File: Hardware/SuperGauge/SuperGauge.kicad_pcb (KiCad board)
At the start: 2 copper layers, 51 x 51 mm, 1 part

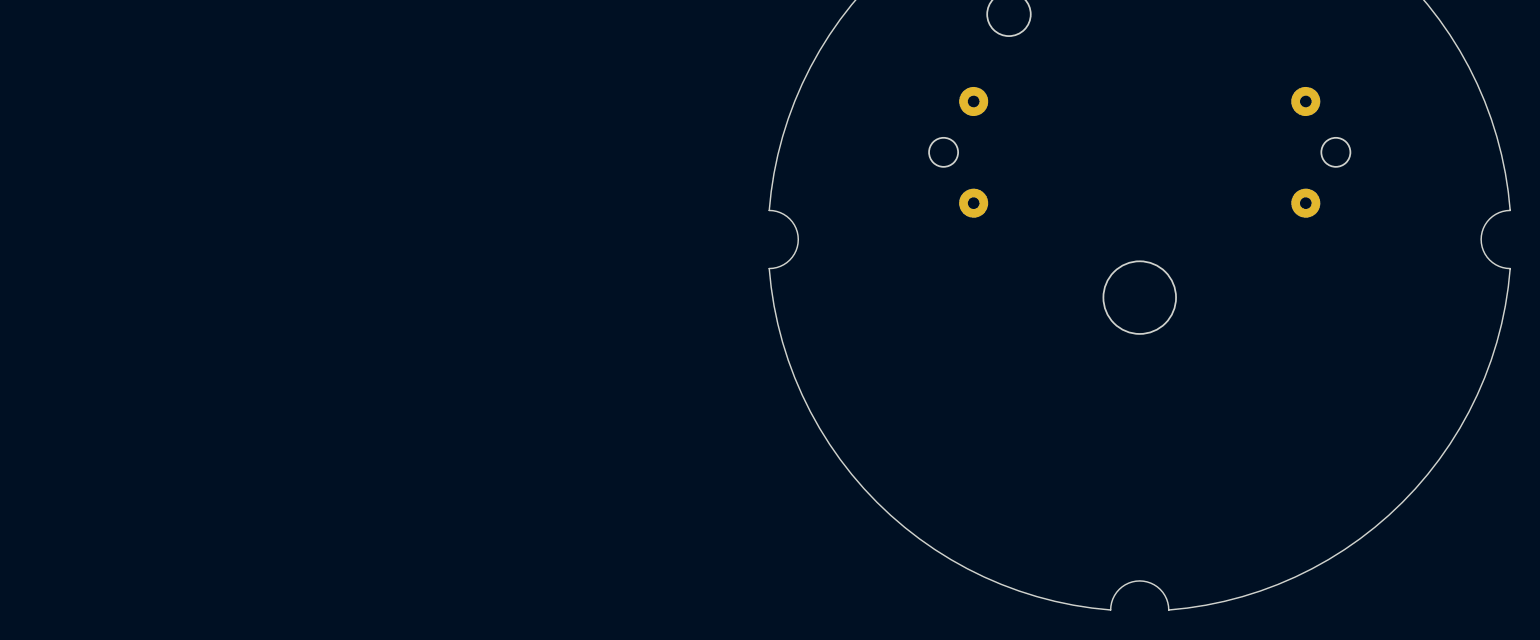
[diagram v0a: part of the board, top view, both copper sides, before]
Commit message: Added in MCU
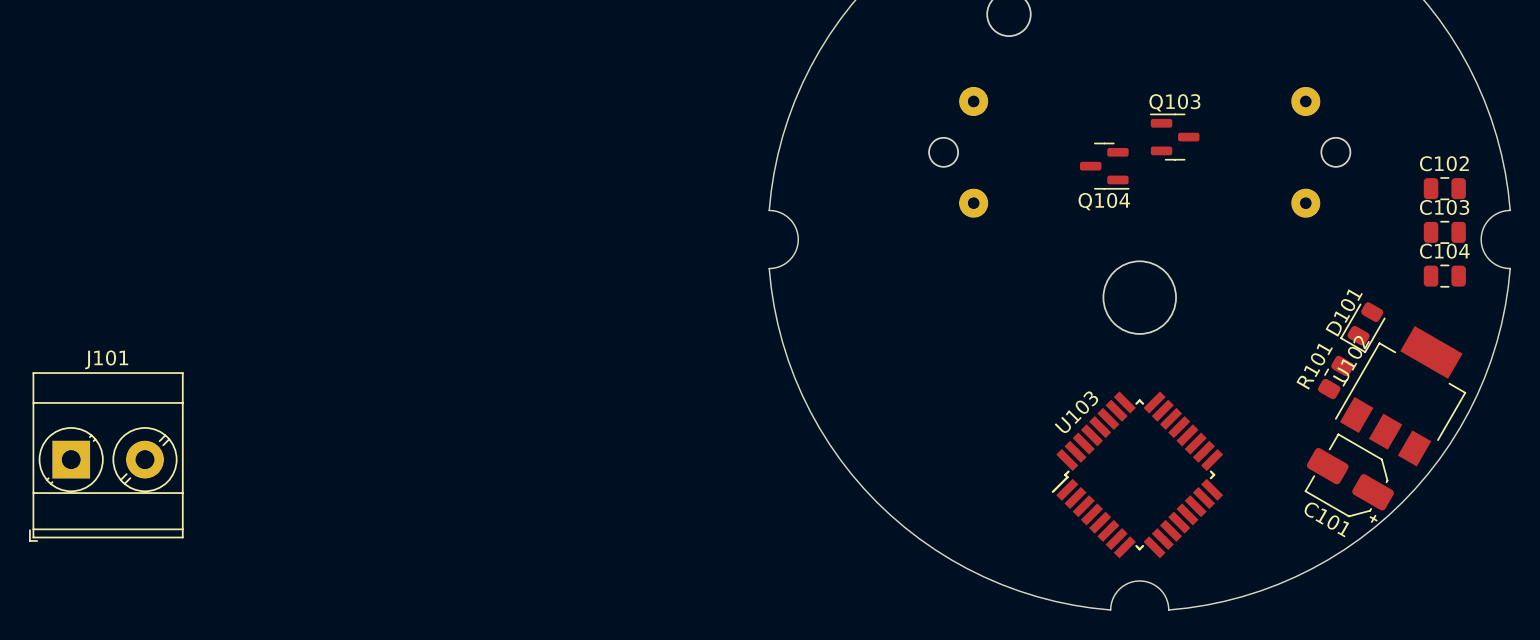
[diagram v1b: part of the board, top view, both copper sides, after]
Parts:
- added C101: 10uf, Capacitor_SMD:CP_Elec_4x3, F.Cu at (164.5, 116.5)
- added C102: 100nF, Capacitor_SMD:C_0805_2012Metric, F.Cu at (171.0, 96.5)
- added C103: 100nF, Capacitor_SMD:C_0805_2012Metric, F.Cu at (171.0, 99.5)
- added C104: 1uF, Capacitor_SMD:C_0805_2012Metric, F.Cu at (171.0, 102.5)
- added D101: PWR, LED_SMD:LED_0805_2012Metric, F.Cu at (165.5, 105.8)
- added J101: 19V Input, TerminalBlock_Phoenix:TerminalBlock_Phoenix_MKDS-3-2-5.08_1x02_P5.08mm_Horizontal, F.Cu at (76.5, 115.2)
- added Q103: MMBT3906, Package_TO_SOT_SMD:SOT-23, F.Cu at (152.4, 93.0)
- added Q104: MMBT3906, Package_TO_SOT_SMD:SOT-23, F.Cu at (147.6, 95.0)
- added R101: 1K, Resistor_SMD:R_0805_2012Metric, F.Cu at (163.5, 109.5)
- added U102: NCV1117ST50T3G, Package_TO_SOT_SMD:SOT-223, F.Cu at (168.5, 110.5)
- added U103: ATmega16U2-A, Package_QFP:TQFP-32_7x7mm_P0.8mm, F.Cu at (150.0, 116.2)
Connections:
- U101 pad 1: unconnected-(U101-Pad1) -> Net-(Q103-C)
- U101 pad 2: unconnected-(U101-Pad2) -> GND
- U101 pad 3: unconnected-(U101-Pad3) -> Net-(Q104-C)
- U101 pad 4: unconnected-(U101-Pad4) -> GND

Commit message: More stuff
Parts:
- removed J101: 19V Input, TerminalBlock_Phoenix:TerminalBlock_Phoenix_MKDS-3-2-5.08_1x02_P5.08mm_Horizontal
- added D102: BACKLIGHTING, LED_THT:LED_D5.0mm_Clear, B.Cu at (129.0, 95.0)
- added D103: BACKLIGHTING, LED_THT:LED_D5.0mm_Clear, B.Cu at (171.0, 95.0)
- added H101: MountingHole, MountingHole:MountingHole_2.5mm, F.Cu at (130.0, 105.0)
- added H102: MountingHole, MountingHole:MountingHole_2.5mm, F.Cu at (170.0, 105.0)
- added J102: MainConn, Connector_JST:JST_EH_B5B-EH-A_1x05_P2.50mm_Vertical, F.Cu at (138.5, 118.5)
- added R102: 1K, Resistor_SMD:R_0805_2012Metric, F.Cu at (132.5, 92.5)
- added R103: 1K, Resistor_SMD:R_0805_2012Metric, F.Cu at (167.5, 92.0)
- U103: value ATmega16U2-A -> ATmega16U2
- moved C101 36.7 mm to (146.5, 84.5), turned to 180 degrees
- moved U102 31.6 mm to (154.8, 82.0), turned to 0 degrees
- moved C104 31.1 mm to (149.0, 80.5), turned to 90 degrees
- moved C102 20.8 mm to (152.5, 87.0)
- moved C103 20.3 mm to (155.0, 112.0), turned to -45 degrees
- moved D101 3.69 mm to (168.5, 108.0), turned to 180 degrees
- moved R101 2.12 mm to (165.0, 108.0), turned to 0 degrees
- turned U103 to -135 degrees
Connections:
- net Net-(J101-Pin_2) renamed +12V
- U103 pad 4: unconnected-(U103-VCC-Pad4) -> +5V
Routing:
- added copper zone on B.Cu, net GND
- added copper zone on F.Cu, net GND
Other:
- board text added: "12V 5V SDA SCL GND"

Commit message: More PCB stuff
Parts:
- added C105: 22pf, Capacitor_SMD:C_0603_1608Metric, F.Cu at (145.2, 109.5)
- added C106: 22pf, Capacitor_SMD:C_0603_1608Metric, F.Cu at (147.5, 107.3)
- added C107: 1u, Capacitor_SMD:C_0805_2012Metric, F.Cu at (191.0, 116.9)
- added D104: STAT, LED_SMD:LED_0805_2012Metric, F.Cu at (195.5, 110.9)
- added J101: USBC, Connector_USB:USB_C_Receptacle_XKB_U262-16XN-4BVC11, F.Cu at (164.5, 115.0)
- added R104: 1K, Resistor_SMD:R_0805_2012Metric, F.Cu at (186.6, 110.9)
- added R106: 5K1, Resistor_SMD:R_0805_2012Metric, F.Cu at (186.6, 116.8)
- added R107: 5K1, Resistor_SMD:R_0805_2012Metric, F.Cu at (186.6, 119.7)
- added Y101: Crystal_GND24, Crystal:Crystal_SMD_3225-4Pin_3.2x2.5mm, F.Cu at (144.4, 106.1)
- moved C103 11.3 mm to (143.8, 111.8), turned to 135 degrees
- moved D101 8.01 mm to (168.1, 100.0)
- moved R101 8.01 mm to (164.6, 100.0)
- moved J102 0.86 mm to (138.1, 119.2)
- moved U103 0.20 mm to (150.0, 116.0), turned to -45 degrees
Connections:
- U103 pad 1: unconnected-(U103-XTAL1-Pad1) -> /XTAL1
- U103 pad 2: unconnected-(U103-PC0/XTAL2-Pad2) -> /XTAL2
- U103 pad 27: unconnected-(U103-UCAP-Pad27) -> Net-(U103-UCAP)
- U103 pad 29: unconnected-(U103-D+-Pad29) -> /USB+
- U103 pad 30: unconnected-(U103-D--Pad30) -> /USB-
- U103 pad 32: unconnected-(U103-AVCC-Pad32) -> +5V
- U103 pad 6: unconnected-(U103-PD0-Pad6) -> Net-(U103-PD0)
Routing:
- net /XTAL1: track 0.00 -> 8.82 mm
- net /XTAL2: track 0.00 -> 5.85 mm
- net GND: track 0.00 -> 3.67 mm, vias 0 -> 5

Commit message: Stuff
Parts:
- removed H101, H102: MountingHole, MountingHole:MountingHole_2.5mm
- added G***: LOGO, KenwoodFox:KITSUNE_LOGO, B.Cu at (146.0, 118.0)
- added J103: Tag Connect, Connector:Tag-Connect_TC2050-IDC-FP_2x05_P1.27mm_Vertical, B.Cu at (130.9, 102.0)
- added R105: 22R, Resistor_SMD:R_0805_2012Metric, F.Cu at (160.6, 109.6)
- added R108: 22R, Resistor_SMD:R_0805_2012Metric, F.Cu at (159.2, 111.0)
- added R109: 10k, Resistor_SMD:R_0805_2012Metric, F.Cu at (156.0, 119.5)
- moved C107 35.0 mm to (156.2, 112.8), turned to -45 degrees
- moved D104 29.0 mm to (168.2, 101.0), turned to 180 degrees
- moved R107 26.6 mm to (160.0, 119.8), turned to 135 degrees
- moved R104 24.0 mm to (164.7, 101.0)
- moved R106 18.4 mm to (169.2, 110.5), turned to 135 degrees
- moved D101 1.26 mm to (168.2, 98.8)
- moved R101 1.26 mm to (164.7, 98.8)
- moved Q104 0.14 mm to (147.7, 94.8)
- moved J102 0.07 mm to (138.1, 119.3)
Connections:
- U103 pad 15: unconnected-(U103-PB1-Pad15) -> /ICSP_SCK
- U103 pad 16: unconnected-(U103-PB2-Pad16) -> /ICSP_MOSI
- U103 pad 17: unconnected-(U103-PB3-Pad17) -> /ICSP_MISO
- U103 pad 24: unconnected-(U103-PC1/~{RESET}-Pad24) -> /ICSP_RST
- U103 pad 29: /USB+ -> Net-(U103-D+)
- U103 pad 30: /USB- -> Net-(U103-D-)
- U103 pad 31: unconnected-(U103-UVCC-Pad31) -> +5V
- U103 pad 7: unconnected-(U103-PD1-Pad7) -> /L1
- U103 pad 8: unconnected-(U103-PD2-Pad8) -> /L2
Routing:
- net +5V: track 0.00 -> 109.5 mm, vias 0 -> 5
- net /ICSP_RST: track 0.00 -> 49.9 mm, vias 0 -> 1
- net /ICSP_MISO: track 0.00 -> 33.8 mm, vias 0 -> 3
- net /ICSP_SCK: track 0.00 -> 32.4 mm, vias 0 -> 1
- net /ICSP_MOSI: track 0.00 -> 29.2 mm, vias 0 -> 3
- net Net-(U103-D+): track 0.00 -> 12.5 mm, vias 0 -> 2
- net Net-(U103-D-): track 0.00 -> 12.1 mm, vias 0 -> 2
- net Net-(J101-CC1): track 0.00 -> 7.86 mm
- net Net-(J101-CC2): track 0.00 -> 7.36 mm
- net /USB+: track 0.00 -> 4.81 mm
- net /USB-: track 0.00 -> 3.95 mm
- net GND: track 3.67 -> 3.02 mm, vias 5 -> 17
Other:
- outline, holes or cut-outs redrawn
- board text added: "Super Gauge ${FULL_REVISION}"
- board text added: "←"

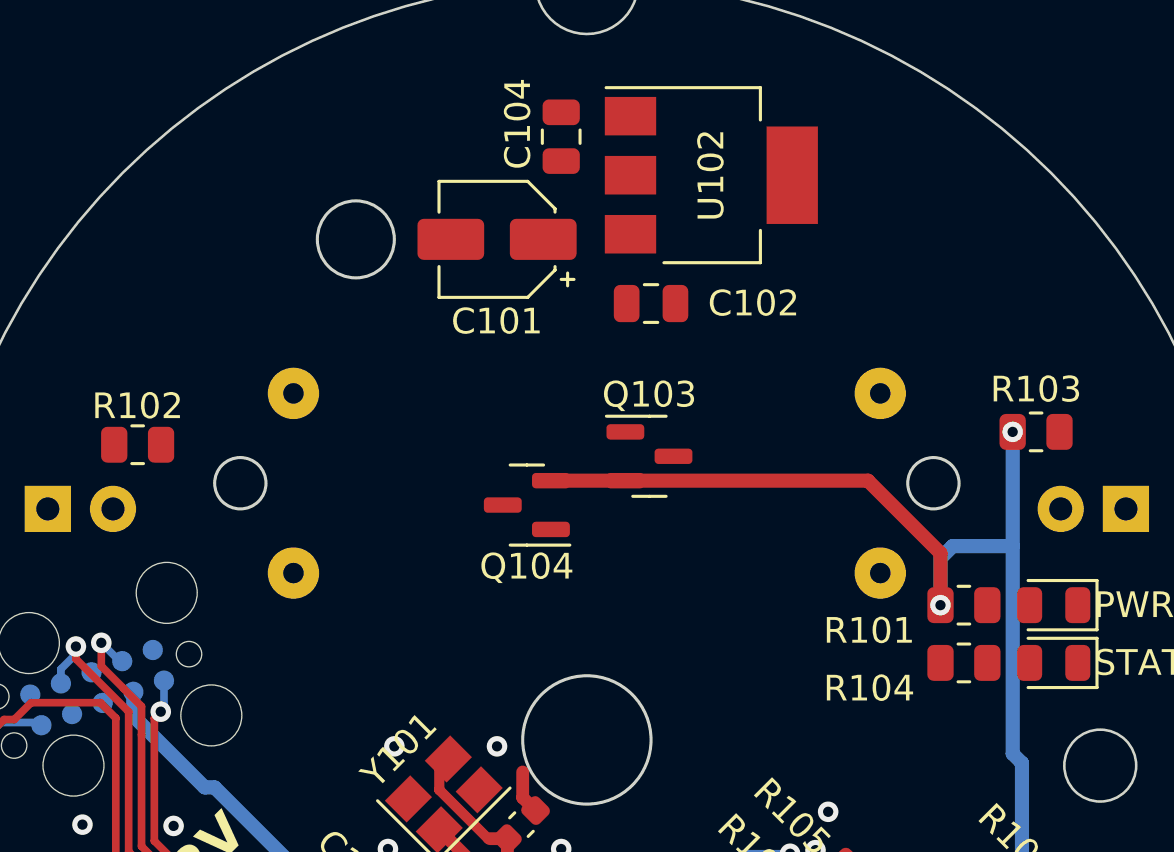
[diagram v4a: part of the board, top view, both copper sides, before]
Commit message: Add motor driver
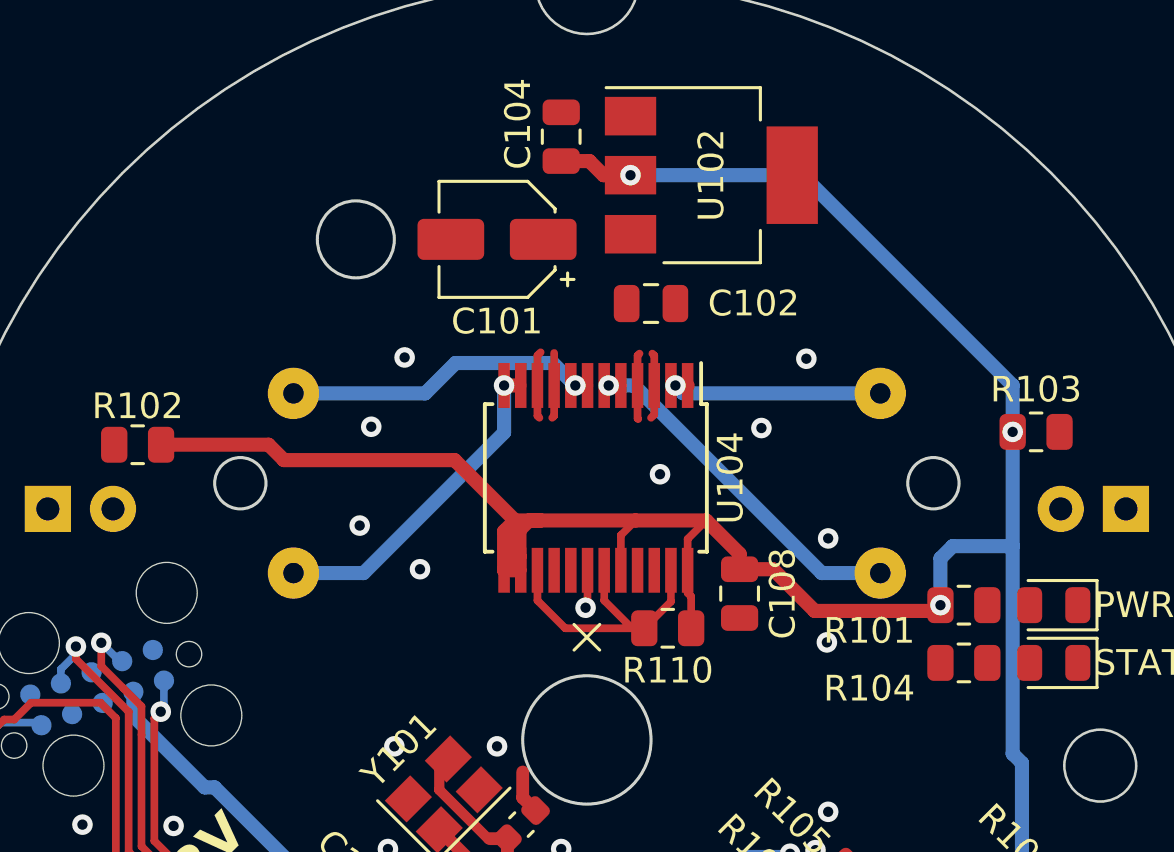
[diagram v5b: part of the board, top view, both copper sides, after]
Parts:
- removed Q103, Q104: MMBT3906, Package_TO_SOT_SMD:SOT-23
- added C108: 1u, Capacitor_SMD:C_0805_2012Metric, F.Cu at (155.9, 98.3)
- added R110: 10k, Resistor_SMD:R_0805_2012Metric, F.Cu at (153.2, 99.7)
- added U104: TB6612FNG, Package_SO:SSOP-24_5.3x8.2mm_P0.65mm, F.Cu at (150.3, 93.8)
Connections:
- U101 pad 2: GND -> Net-(U101-Pad2)
- U101 pad 4: GND -> Net-(U101-Pad4)
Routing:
- net +5V: track 109.5 -> 161.0 mm, vias 5 -> 6
- net Net-(U101-Pad2): track 0.00 -> 14.0 mm, vias 0 -> 1
- net Net-(U101-Pad3): track 0.00 -> 12.9 mm, vias 0 -> 1
- net Net-(U101-Pad4): track 0.00 -> 12.3 mm, vias 0 -> 1
- net GND: track 3.02 -> 15.1 mm, vias 17 -> 27
- net Net-(U104-PWMA): track 0.00 -> 11.7 mm
- net Net-(U101-Pad1): track 0.00 -> 8.58 mm, vias 0 -> 1

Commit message: Connect all
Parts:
- moved C101 180.2 mm to (-3.48, -15.5)
- moved C102 180.2 mm to (2.52, -13.0)
- moved C103 180.2 mm to (-6.23, 11.8)
- moved C104 180.2 mm to (-0.98, -19.5)
- moved C107 180.2 mm to (6.27, 12.8)
- moved D101 180.2 mm to (18.2, -1.23)
- moved D102 180.2 mm to (-21.0, -4.97)
- moved D103 180.2 mm to (21.0, -4.97)
- moved D104 180.2 mm to (18.2, 1.02)
- moved G*** 180.2 mm to (-3.98, 18.0)
- moved J101 180.2 mm to (14.5, 15.0)
- moved R101 180.2 mm to (14.7, -1.23)
- moved R102 180.2 mm to (-17.5, -7.47)
- moved R103 180.2 mm to (17.5, -7.97)
- moved R104 180.2 mm to (14.7, 1.02)
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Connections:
- U103 pad 18: unconnected-(U103-PB4-Pad18) -> /SCL
- U103 pad 19: unconnected-(U103-PB5-Pad19) -> /SDA
- U103 pad 23: unconnected-(U103-PC6-Pad23) -> /BIN2
- U103 pad 25: unconnected-(U103-PC5-Pad25) -> /BIN1
- U103 pad 26: unconnected-(U103-PC4-Pad26) -> /AIN2
- U103 pad 5: unconnected-(U103-PC2-Pad5) -> /AIN1
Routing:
- net +12V: track 0.00 -> 55.7 mm, vias 0 -> 1
- net Net-(U103-PD0): track 0.00 -> 33.4 mm, vias 0 -> 4
- net /BIN2: track 0.00 -> 31.1 mm, vias 0 -> 4
- net /BIN1: track 0.00 -> 28.8 mm, vias 0 -> 4
- net /AIN2: track 0.00 -> 26.4 mm, vias 0 -> 2
- net /AIN1: track 0.00 -> 25.0 mm, vias 0 -> 2
- net /SDA: track 0.00 -> 19.6 mm, vias 0 -> 1
- net /SCL: track 0.00 -> 16.6 mm, vias 0 -> 1
- net GND: track 15.1 -> 21.7 mm, vias 27 -> 38
- net +5V: track 161.0 -> 167.4 mm, vias 6 -> 7
- net /ICSP_RST: track 49.9 -> 43.8 mm
- net Net-(D103-A): track 0.00 -> 3.02 mm
- net Net-(D102-A): track 0.00 -> 2.52 mm
- net Net-(U103-UCAP): track 0.00 -> 2.48 mm
- net Net-(D104-A): track 0.00 -> 1.65 mm
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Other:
- outline, holes or cut-outs redrawn

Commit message: Fix DRC
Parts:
- removed U102: NCV1117ST50T3G, Package_TO_SOT_SMD:SOT-223
- added D105: MBR0520LT, Diode_SMD:D_SOD-123, F.Cu at (13.7, 5.30)
- added U105: LM1117MP-5.0, Package_TO_SOT_SMD:SOT-223-3_TabPin2, F.Cu at (4.85, -17.9)
- moved R107 0.78 mm to (10.6, 20.3)
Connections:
- J101 pad A4: +5V -> Net-(D105-A)
- J101 pad A9: +5V -> Net-(D105-A)
- J101 pad B4: +5V -> Net-(D105-A)
- J101 pad B9: +5V -> Net-(D105-A)
- U103 pad 7: /L1 -> unconnected-(U103-PD1-Pad7)
- U103 pad 8: /L2 -> unconnected-(U103-PD2-Pad8)
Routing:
- net Net-(D105-A): track 0.00 -> 19.7 mm, vias 0 -> 2
- net +5V: track 167.4 -> 158.9 mm
- net GND: track 21.7 -> 24.6 mm, vias 38 -> 39

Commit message: RC time
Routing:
- net GND: track 24.6 -> 24.5 mm, vias 39 -> 42
